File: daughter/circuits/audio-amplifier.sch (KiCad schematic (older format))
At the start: 28 parts, among them J12 AudioJack_3.5TRS, J13 AudioJack_3.5TRS, J14 Conn_01x05, T1 Audio_Transformer, T2 Audio_Transformer, T3 Audio_Transformer, T4 Audio_Transformer, U7 TDA7851F

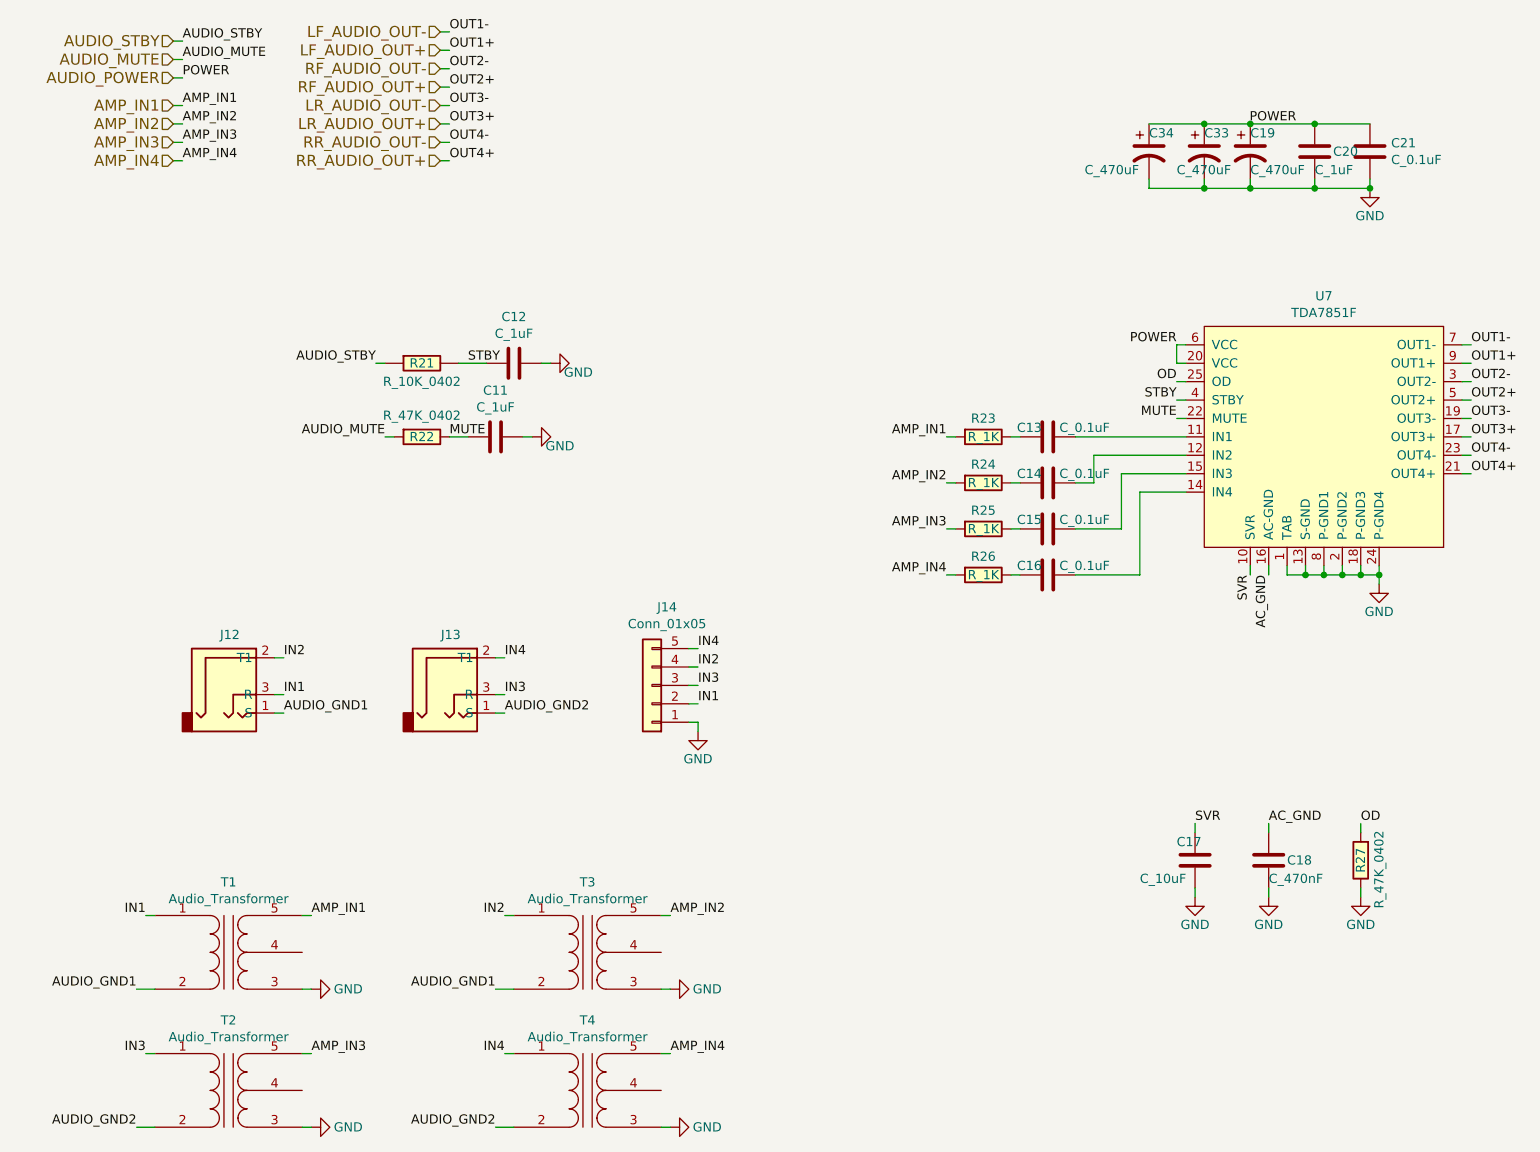
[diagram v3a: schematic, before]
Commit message: Added external amp trigger code and circuit to PCB. Made some layout modifications.
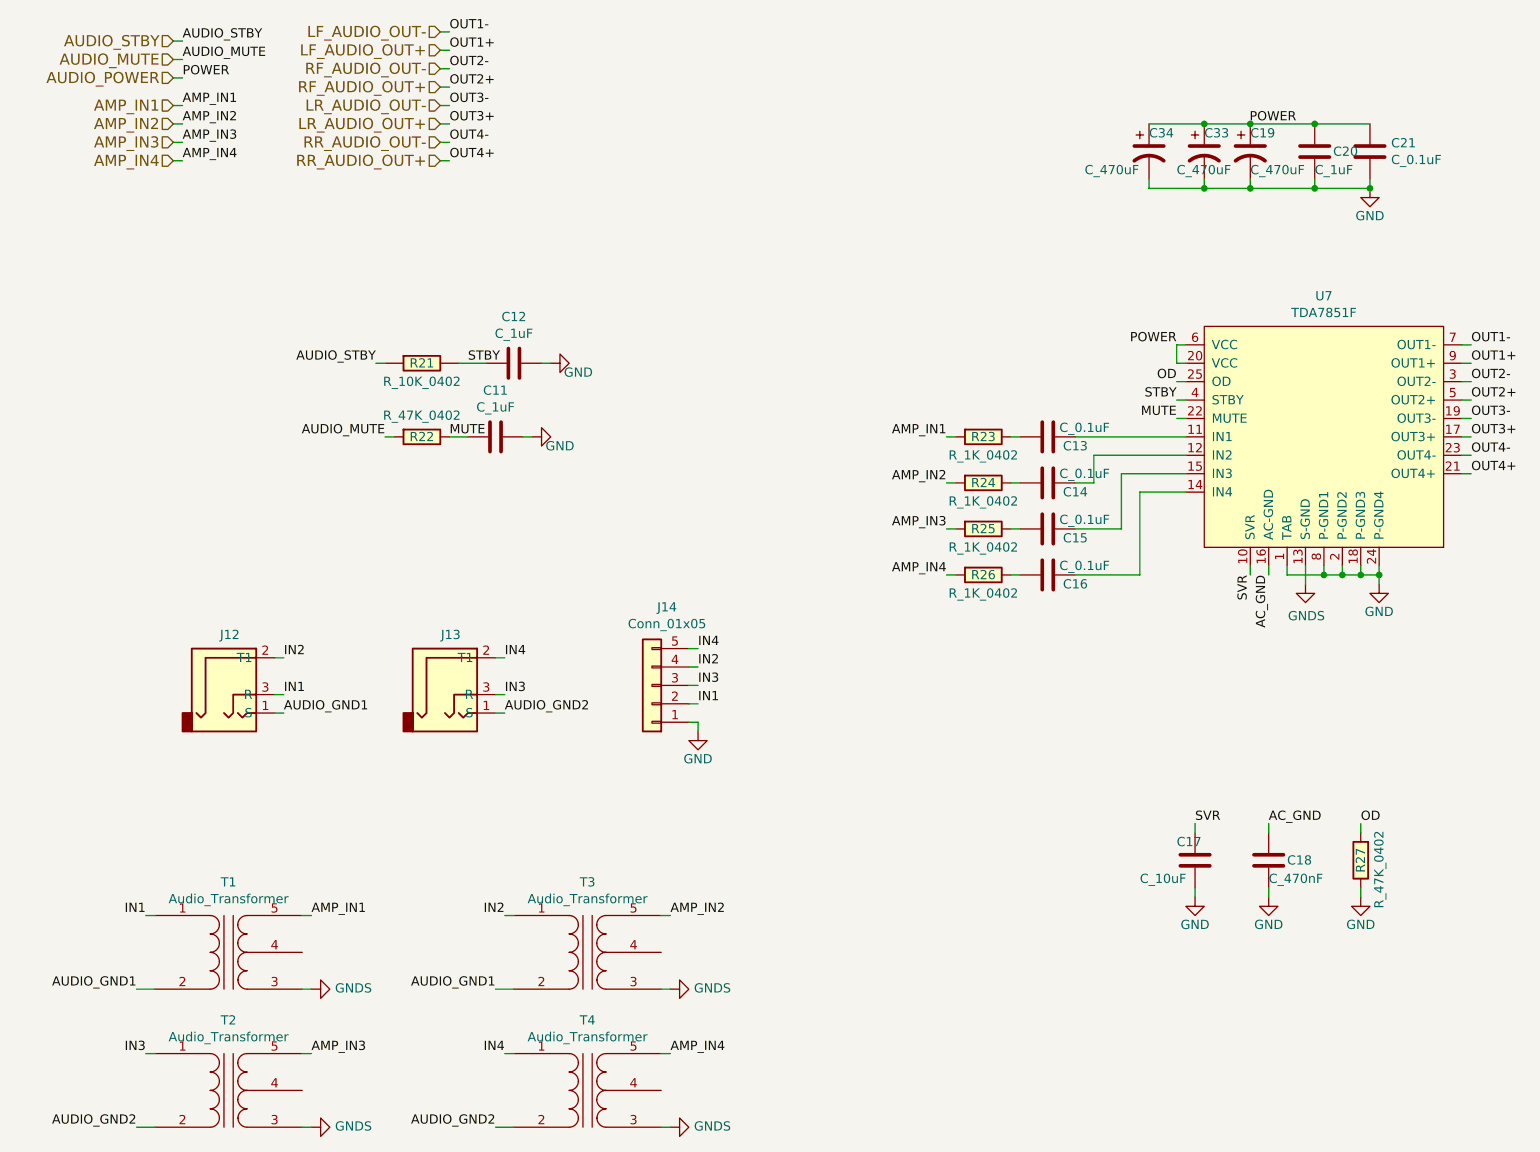
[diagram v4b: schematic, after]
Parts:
- removed R23, R24, R25, R26: R_1K, Resistor_SMD:R_0603_1608Metric_Pad0.98x0.95mm_HandSolder, symbol open-dash-daughterboard-rescue:R_1K-Open_Automation
- added R23, R24, R25, R26: R_1K_0402, Resistor_SMD:R_0402_1005Metric_Pad0.72x0.64mm_HandSolder, symbol Open_Automation:R_1K_0402
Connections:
- net AMP_IN1: now also R23.2
- net AMP_IN2: now also R24.2
- net AMP_IN3: now also R25.2
- net AMP_IN4: now also R26.2
- net GND: no longer T1.3 (SA), T2.3 (SA), T3.3 (SA), T4.3 (SA), U7.13 (S-GND)
- net at C13.2: now also R23.1
- net at C14.2: now also R24.1
- net at C15.2: now also R25.1
- net at C16.2: now also R26.1
- new net GNDS: T1.3 (SA), T2.3 (SA), T3.3 (SA), T4.3 (SA), U7.13 (S-GND)
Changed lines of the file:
@@
 Connection ~ 8100 3950
 Wire Wire Line
-	7900 3900 7900 3950
-Wire Wire Line
-	7900 3950 8000 3950
-Connection ~ 8000 3950
-Wire Wire Line
 	7800 3900 7800 3950
-Wire Wire Line
-	7800 3950 7900 3950
-Connection ~ 7900 3950
 Wire Wire Line
 	7250 2800 7200 2800
@@
 Connection ~ 8250 1850
 $Comp
-L open-dash-daughterboard-rescue:R_1K-Open_Automation R23
-U 1 1 5CC13A39
-P 6150 3200
-F 0 "R23" V 6050 3200 50  0000 C CNN
-F 1 "R_1K" V 6150 3200 50  0000 C CNN
-F 2 "Resistor_SMD:R_0603_1608Metric_Pad0.98x0.95mm_HandSolder" V 6080 3200 50  0001 C CNN
-F 3 "https://www.digikey.com/product-detail/en/panasonic-electronic-components/ERJ-3GEYJ102V/P1.0KGDKR-ND/577615" V 6230 3200 50  0001 C CNN
-F 4 "ERJ-3GEYJ102V" V 6330 3300 60  0001 C CNN "Part Number"
-F 5 " C21190" H 1650 -1150 50  0001 C CNN "LCSC"
-	1    6150 3200
-	0    1    1    0
-$EndComp
-$Comp
 L open-dash-daughterboard-rescue:GND-power #PWR059
 U 1 1 5CC4D3C7
@@
 	1    0    0    -1
 $EndComp
-$Comp
-L open-dash-daughterboard-rescue:R_1K-Open_Automation R24
-U 1 1 60274D86
-P 6150 3450
-F 0 "R24" V 6050 3450 50  0000 C CNN
-F 1 "R_1K" V 6150 3450 50  0000 C CNN
-F 2 "Resistor_SMD:R_0603_1608Metric_Pad0.98x0.95mm_HandSolder" V 6080 3450 50  0001 C CNN
-F 3 "https://www.digikey.com/product-detail/en/panasonic-electronic-components/ERJ-3GEYJ102V/P1.0KGDKR-ND/577615" V 6230 3450 50  0001 C CNN
-F 4 "ERJ-3GEYJ102V" V 6330 3550 60  0001 C CNN "Part Number"
-F 5 " C21190" H 1650 -1150 50  0001 C CNN "LCSC"
-	1    6150 3450
-	0    1    1    0
-$EndComp
-$Comp
-L open-dash-daughterboard-rescue:R_1K-Open_Automation R25
-U 1 1 6027525B
-P 6150 3700
-F 0 "R25" V 6050 3700 50  0000 C CNN
-F 1 "R_1K" V 6150 3700 50  0000 C CNN
-F 2 "Resistor_SMD:R_0603_1608Metric_Pad0.98x0.95mm_HandSolder" V 6080 3700 50  0001 C CNN
-F 3 "https://www.digikey.com/product-detail/en/panasonic-electronic-components/ERJ-3GEYJ102V/P1.0KGDKR-ND/577615" V 6230 3700 50  0001 C CNN
-F 4 "ERJ-3GEYJ102V" V 6330 3800 60  0001 C CNN "Part Number"
-F 5 " C21190" H 1650 -1150 50  0001 C CNN "LCSC"
-	1    6150 3700
-	0    1    1    0
-$EndComp
-$Comp
-L open-dash-daughterboard-rescue:R_1K-Open_Automation R26
-U 1 1 602754FA
-P 6150 3950
-F 0 "R26" V 6050 3950 50  0000 C CNN
-F 1 "R_1K" V 6150 3950 50  0000 C CNN
-F 2 "Resistor_SMD:R_0603_1608Metric_Pad0.98x0.95mm_HandSolder" V 6080 3950 50  0001 C CNN
-F 3 "https://www.digikey.com/product-detail/en/panasonic-electronic-components/ERJ-3GEYJ102V/P1.0KGDKR-ND/577615" V 6230 3950 50  0001 C CNN
-F 4 "ERJ-3GEYJ102V" V 6330 4050 60  0001 C CNN "Part Number"
-F 5 " C21190" H 1650 -1150 50  0001 C CNN "LCSC"
-	1    6150 3950
-	0    1    1    0
-$EndComp
 Text HLabel 1750 1500 0    60   Input ~ 0
 AMP_IN2
@@
 Text Label 3550 4700 0    50   ~ 0
 AUDIO_GND2
-$Comp
-L open-dash-daughterboard-rescue:GND-power #PWR056
-U 1 1 62C04F2E
-P 2500 6200
-F 0 "#PWR056" H 2500 5950 50  0001 C CNN
-F 1 "GND" V 2500 6000 50  0000 C CNN
-F 2 "" H 2500 6200 50  0000 C CNN
-F 3 "" H 2500 6200 50  0000 C CNN
-	1    2500 6200
-	0    -1   -1   0
-$EndComp
 Wire Wire Line
 	2500 6200 2450 6200
@@
 Wire Wire Line
 	1550 6950 1650 6950
-$Comp
-L open-dash-daughterboard-rescue:GND-power #PWR057
-U 1 1 62C27863
-P 2500 6950
-F 0 "#PWR057" H 2500 6700 50  0001 C CNN
-F 1 "GND" V 2500 6750 50  0000 C CNN
-F 2 "" H 2500 6950 50  0000 C CNN
-F 3 "" H 2500 6950 50  0000 C CNN
-	1    2500 6950
-	0    -1   -1   0
-$EndComp
 Wire Wire Line
 	2500 6950 2450 6950
@@
 Wire Wire Line
 	3500 6200 3600 6200
-$Comp
-L open-dash-daughterboard-rescue:GND-power #PWR060
-U 1 1 62C31FFF
-P 4450 6200
-F 0 "#PWR060" H 4450 5950 50  0001 C CNN
-F 1 "GND" V 4450 6000 50  0000 C CNN
-F 2 "" H 4450 6200 50  0000 C CNN
-F 3 "" H 4450 6200 50  0000 C CNN
-	1    4450 6200
-	0    -1   -1   0
-$EndComp
 Wire Wire Line
 	4450 6200 4400 6200
@@
 Wire Wire Line
 	3500 6950 3600 6950
-$Comp
-L open-dash-daughterboard-rescue:GND-power #PWR061
-U 1 1 62C3201A
-P 4450 6950
-F 0 "#PWR061" H 4450 6700 50  0001 C CNN
-F 1 "GND" V 4450 6750 50  0000 C CNN
-F 2 "" H 4450 6950 50  0000 C CNN
-F 3 "" H 4450 6950 50  0000 C CNN
-	1    4450 6950
-	0    -1   -1   0
-$EndComp
 Wire Wire Line
 	4450 6950 4400 6950
@@
 U 1 1 605275DE
 P 6500 3200
-F 0 "C13" V 6450 3100 50  0000 C CNN
+F 0 "C13" V 6550 3350 50  0000 C CNN
 F 1 "C_0.1uF" V 6450 3400 50  0000 C CNN
 F 2 "Capacitor_SMD:C_0402_1005Metric_Pad0.74x0.62mm_HandSolder" H 6600 3500 50  0001 C CNN
@@
 U 1 1 6052A102
 P 6500 3450
-F 0 "C14" V 6450 3350 50  0000 C CNN
+F 0 "C14" V 6550 3600 50  0000 C CNN
 F 1 "C_0.1uF" V 6450 3650 50  0000 C CNN
 F 2 "Capacitor_SMD:C_0402_1005Metric_Pad0.74x0.62mm_HandSolder" H 6600 3750 50  0001 C CNN
@@
 U 1 1 6052ABFB
 P 6500 3700
-F 0 "C15" V 6450 3600 50  0000 C CNN
+F 0 "C15" V 6550 3850 50  0000 C CNN
 F 1 "C_0.1uF" V 6450 3900 50  0000 C CNN
 F 2 "Capacitor_SMD:C_0402_1005Metric_Pad0.74x0.62mm_HandSolder" H 6600 4000 50  0001 C CNN
@@
 U 1 1 6052AC07
 P 6500 3950
-F 0 "C16" V 6450 3850 50  0000 C CNN
+F 0 "C16" V 6550 4100 50  0000 C CNN
 F 1 "C_0.1uF" V 6450 4150 50  0000 C CNN
 F 2 "Capacitor_SMD:C_0402_1005Metric_Pad0.74x0.62mm_HandSolder" H 6600 4250 50  0001 C CNN
@@
 Text Label 4450 6550 0    50   ~ 0
 AMP_IN4
+$Comp
+L Open_Automation:R_1K_0402 R23
+U 1 1 619ADBEE
+P 6150 3200
+F 0 "R23" V 6150 3200 50  0000 C CNN
+F 1 "R_1K_0402" V 6250 3200 50  0000 C CNN
+F 2 "Resistor_SMD:R_0402_1005Metric_Pad0.72x0.64mm_HandSolder" V 6080 3200 50  0001 C CNN
+F 3 "https://www.digikey.com/product-detail/en/panasonic-electronic-components/ERJ-3GEYJ102V/P1.0KGDKR-ND/577615" V 6230 3200 50  0001 C CNN
+F 4 "0402WGF1001TCE" V 6330 3300 60  0001 C CNN "Part Number"
+F 5 "C11702" H 6150 3200 50  0001 C CNN "LCSC"
+	1    6150 3200
+	0    1    1    0
+$EndComp
+$Comp
+L Open_Automation:R_1K_0402 R24
+U 1 1 619B019A
+P 6150 3450
+F 0 "R24" V 6150 3450 50  0000 C CNN
+F 1 "R_1K_0402" V 6250 3450 50  0000 C CNN
+F 2 "Resistor_SMD:R_0402_1005Metric_Pad0.72x0.64mm_HandSolder" V 6080 3450 50  0001 C CNN
+F 3 "https://www.digikey.com/product-detail/en/panasonic-electronic-components/ERJ-3GEYJ102V/P1.0KGDKR-ND/577615" V 6230 3450 50  0001 C CNN
+F 4 "0402WGF1001TCE" V 6330 3550 60  0001 C CNN "Part Number"
+F 5 "C11702" H 6150 3450 50  0001 C CNN "LCSC"
+	1    6150 3450
+	0    1    1    0
+$EndComp
+$Comp
+L Open_Automation:R_1K_0402 R25
+U 1 1 619B0C77
+P 6150 3700
+F 0 "R25" V 6150 3700 50  0000 C CNN
+F 1 "R_1K_0402" V 6250 3700 50  0000 C CNN
+F 2 "Resistor_SMD:R_0402_1005Metric_Pad0.72x0.64mm_HandSolder" V 6080 3700 50  0001 C CNN
+F 3 "https://www.digikey.com/product-detail/en/panasonic-electronic-components/ERJ-3GEYJ102V/P1.0KGDKR-ND/577615" V 6230 3700 50  0001 C CNN
+F 4 "0402WGF1001TCE" V 6330 3800 60  0001 C CNN "Part Number"
+F 5 "C11702" H 6150 3700 50  0001 C CNN "LCSC"
+	1    6150 3700
+	0    1    1    0
+$EndComp
+$Comp
+L Open_Automation:R_1K_0402 R26
+U 1 1 619B1093
+P 6150 3950
+F 0 "R26" V 6150 3950 50  0000 C CNN
+F 1 "R_1K_0402" V 6250 3950 50  0000 C CNN
+F 2 "Resistor_SMD:R_0402_1005Metric_Pad0.72x0.64mm_HandSolder" V 6080 3950 50  0001 C CNN
+F 3 "https://www.digikey.com/product-detail/en/panasonic-electronic-components/ERJ-3GEYJ102V/P1.0KGDKR-ND/577615" V 6230 3950 50  0001 C CNN
+F 4 "0402WGF1001TCE" V 6330 4050 60  0001 C CNN "Part Number"
+F 5 "C11702" H 6150 3950 50  0001 C CNN "LCSC"
+	1    6150 3950
+	0    1    1    0
+$EndComp
+$Comp
+L power:GNDS #PWR0151
+U 1 1 619E09BC
+P 7900 4000
+F 0 "#PWR0151" H 7900 3750 50  0001 C CNN
+F 1 "GNDS" H 7905 3827 50  0000 C CNN
+F 2 "" H 7900 4000 50  0001 C CNN
+F 3 "" H 7900 4000 50  0001 C CNN
+	1    7900 4000
+	1    0    0    -1
+$EndComp
+Wire Wire Line
+	7900 3900 7900 4000
+Connection ~ 8000 3950
+Wire Wire Line
+	7800 3950 8000 3950
+$Comp
+L power:GNDS #PWR0152
+U 1 1 619EC47D
+P 2500 6950
+F 0 "#PWR0152" H 2500 6700 50  0001 C CNN
+F 1 "GNDS" V 2505 6822 50  0000 R CNN
+F 2 "" H 2500 6950 50  0001 C CNN
+F 3 "" H 2500 6950 50  0001 C CNN
+	1    2500 6950
+	0    -1   -1   0
+$EndComp
+$Comp
+L power:GNDS #PWR0153
+U 1 1 619F385D
+P 2500 6200
+F 0 "#PWR0153" H 2500 5950 50  0001 C CNN
+F 1 "GNDS" V 2505 6072 50  0000 R CNN
+F 2 "" H 2500 6200 50  0001 C CNN
+F 3 "" H 2500 6200 50  0001 C CNN
+	1    2500 6200
+	0    -1   -1   0
+$EndComp
+$Comp
+L power:GNDS #PWR0154
+U 1 1 619F3E43
+P 4450 6200
+F 0 "#PWR0154" H 4450 5950 50  0001 C CNN
+F 1 "GNDS" V 4455 6072 50  0000 R CNN
+F 2 "" H 4450 6200 50  0001 C CNN
+F 3 "" H 4450 6200 50  0001 C CNN
+	1    4450 6200
+	0    -1   -1   0
+$EndComp
+$Comp
+L power:GNDS #PWR0155
+U 1 1 619F550E
+P 4450 6950
+F 0 "#PWR0155" H 4450 6700 50  0001 C CNN
+F 1 "GNDS" V 4455 6822 50  0000 R CNN
+F 2 "" H 4450 6950 50  0001 C CNN
+F 3 "" H 4450 6950 50  0001 C CNN
+	1    4450 6950
+	0    -1   -1   0
+$EndComp
 $EndSCHEMATC
